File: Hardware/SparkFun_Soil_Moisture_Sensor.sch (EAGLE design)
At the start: 16 parts, among them J1 GATORGATOR_MINI, J2 GATORGATOR_MINI, J3 GATORGATOR_MINI, Q1 2N3904

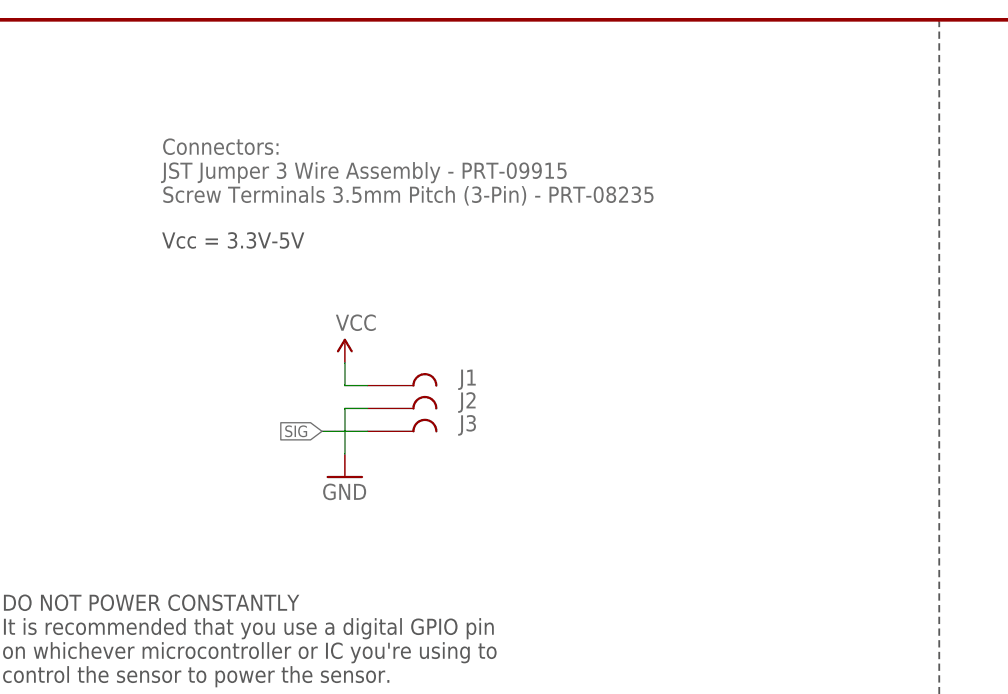
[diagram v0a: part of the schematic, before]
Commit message: adding protection circuitry
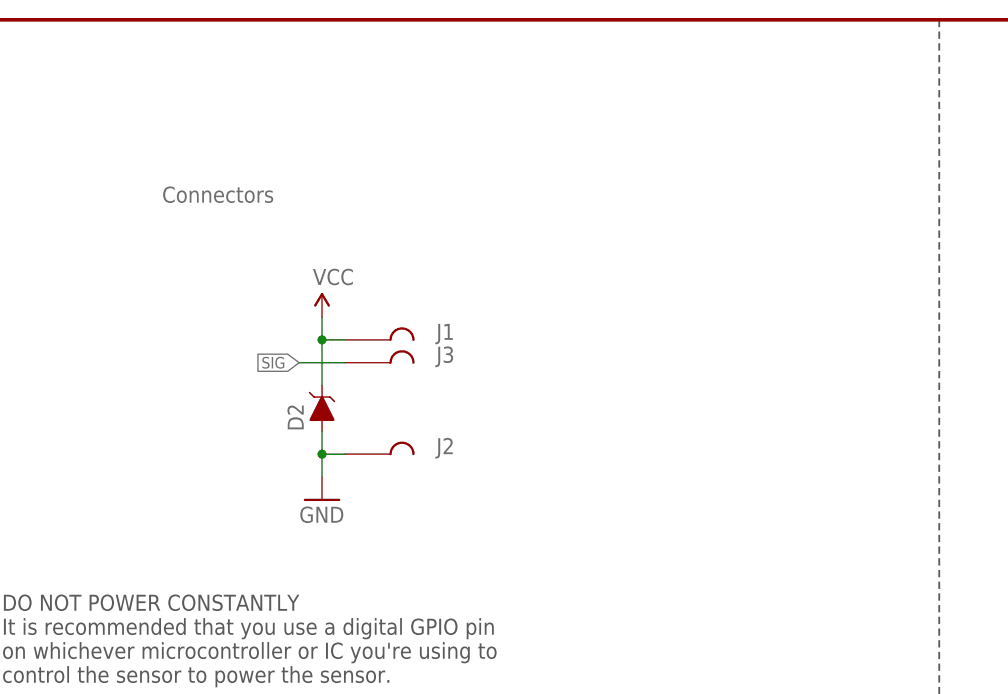
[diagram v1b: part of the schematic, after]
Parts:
- added D2: 3.6V, SparkFun-DiscreteSemi:DIODE-ZENER-BZT52C3V6S
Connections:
- net GND: now also D2.A
- net VCC: now also D2.C
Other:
- note added: "Connectors"
- note removed: "Connectors: JST Jumper 3 Wire Assembly - PRT-09915 Screw Terminals 3.5mm Pitch (3-Pin) - PRT-08235"
- note removed: "Vcc = 3.3V-5V"
- moved on the sheet: J1, J2, J3
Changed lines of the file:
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@@
 <part name="FID4" library="SparkFun-Aesthetics" deviceset="FIDUCIAL" device="1X2"/>
 <part name="LOGO3" library="SparkFun-Aesthetics" deviceset="REVISION" device=""/>
+<part name="D2" library="SparkFun-DiscreteSemi" deviceset="DIODE-ZENER" device="-BZT52C3V6S" value="3.6V"/>
 </parts>
 <sheets>
@@
 The big variable is the composition of the soil itself (especially salts), so ideally you would calibrate for each type of soil.
 -Rob Faludi</text>
-<text x="30.48" y="165.1" size="1.778" layer="95" font="vector">Connectors:
-JST Jumper 3 Wire Assembly - PRT-09915
-Screw Terminals 3.5mm Pitch (3-Pin) - PRT-08235</text>
+<text x="30.48" y="165.1" size="1.778" layer="95" font="vector">Connectors</text>
 <text x="167.64" y="172.72" size="1.778" layer="95" font="vector">Probe Circuit</text>
-<text x="30.48" y="160.02" size="1.778" layer="97" font="vector">Vcc = 3.3V-5V</text>
 <text x="12.7" y="111.76" size="1.778" layer="97" font="vector">DO NOT POWER CONSTANTLY
 It is recommended that you use a digital GPIO pin
@@
 <attribute name="VALUE" x="184.404" y="161.036" size="1.778" layer="96" font="vector"/>
 </instance>
-<instance part="SUPPLY3" gate="G$1" x="50.8" y="147.32" smashed="yes">
-<attribute name="VALUE" x="49.784" y="150.876" size="1.778" layer="96" font="vector"/>
+<instance part="SUPPLY3" gate="G$1" x="48.26" y="152.4" smashed="yes">
+<attribute name="VALUE" x="47.244" y="155.956" size="1.778" layer="96" font="vector"/>
 </instance>
-<instance part="GND2" gate="1" x="50.8" y="134.62" smashed="yes">
-<attribute name="VALUE" x="48.26" y="132.08" size="1.778" layer="96" font="vector"/>
+<instance part="GND2" gate="1" x="48.26" y="132.08" smashed="yes">
+<attribute name="VALUE" x="45.72" y="129.54" size="1.778" layer="96" font="vector"/>
 </instance>
 <instance part="FRAME1" gate="G$1" x="0" y="0" smashed="yes"/>
@@
 <instance part="FID1" gate="G$1" x="137.16" y="27.94" smashed="yes"/>
 <instance part="FID2" gate="G$1" x="142.24" y="27.94" smashed="yes"/>
-<instance part="J1" gate="G$1" x="55.88" y="144.78" smashed="yes">
-<attribute name="NAME" x="63.5" y="144.78" size="1.778" layer="95" font="vector"/>
+<instance part="J1" gate="G$1" x="53.34" y="149.86" smashed="yes">
+<attribute name="NAME" x="60.96" y="149.86" size="1.778" layer="95" font="vector"/>
 </instance>
-<instance part="J2" gate="G$1" x="55.88" y="142.24" smashed="yes">
-<attribute name="NAME" x="63.5" y="142.24" size="1.778" layer="95" font="vector"/>
+<instance part="J2" gate="G$1" x="53.34" y="137.16" smashed="yes">
+<attribute name="NAME" x="60.96" y="137.16" size="1.778" layer="95" font="vector"/>
 </instance>
-<instance part="J3" gate="G$1" x="55.88" y="139.7" smashed="yes">
-<attribute name="NAME" x="63.5" y="139.7" size="1.778" layer="95" font="vector"/>
+<instance part="J3" gate="G$1" x="53.34" y="147.32" smashed="yes">
+<attribute name="NAME" x="60.96" y="147.32" size="1.778" layer="95" font="vector"/>
 </instance>
 <instance part="FID3" gate="G$1" x="137.16" y="22.86" smashed="yes"/>
 <instance part="FID4" gate="G$1" x="142.24" y="22.86" smashed="yes"/>
 <instance part="LOGO3" gate="G$1" x="148.59" y="7.366" smashed="yes"/>
+<instance part="D2" gate="G$1" x="48.26" y="142.24" smashed="yes" rot="R90">
+<attribute name="NAME" x="46.228" y="139.7" size="1.778" layer="95" font="vector" rot="R90"/>
+</instance>
 </instances>
 <busses>
@@
 </segment>
 <segment>
-<wire x1="53.34" y1="139.7" x2="48.26" y2="139.7" width="0.1524" layer="91"/>
-<label x="48.26" y="139.7" size="1.27" layer="95" font="vector" rot="R180" xref="yes"/>
+<label x="45.72" y="147.32" size="1.27" layer="95" font="vector" rot="R180" xref="yes"/>
 <pinref part="J3" gate="G$1" pin="P$1"/>
+<wire x1="50.8" y1="147.32" x2="45.72" y2="147.32" width="0.1524" layer="91"/>
 </segment>
 </net>
@@
 <segment>
 <pinref part="SUPPLY3" gate="G$1" pin="VCC"/>
-<wire x1="53.34" y1="144.78" x2="50.8" y2="144.78" width="0.1524" layer="91"/>
-<wire x1="50.8" y1="144.78" x2="50.8" y2="147.32" width="0.1524" layer="91"/>
+<wire x1="50.8" y1="149.86" x2="48.26" y2="149.86" width="0.1524" layer="91"/>
+<wire x1="48.26" y1="149.86" x2="48.26" y2="152.4" width="0.1524" layer="91"/>
 <pinref part="J1" gate="G$1" pin="P$1"/>
+<pinref part="D2" gate="G$1" pin="C"/>
+<wire x1="48.26" y1="149.86" x2="48.26" y2="144.78" width="0.1524" layer="91"/>
+<junction x="48.26" y="149.86"/>
 </segment>
 <segment>
@@
 <segment>
 <pinref part="J2" gate="G$1" pin="P$1"/>
-<wire x1="53.34" y1="142.24" x2="50.8" y2="142.24" width="0.1524" layer="91"/>
 <pinref part="GND2" gate="1" pin="GND"/>
-<wire x1="50.8" y1="142.24" x2="50.8" y2="137.16" width="0.1524" layer="91"/>
+<wire x1="50.8" y1="137.16" x2="48.26" y2="137.16" width="0.1524" layer="91"/>
+<wire x1="48.26" y1="137.16" x2="48.26" y2="134.62" width="0.1524" layer="91"/>
+<pinref part="D2" gate="G$1" pin="A"/>
+<wire x1="48.26" y1="139.7" x2="48.26" y2="137.16" width="0.1524" layer="91"/>
+<junction x="48.26" y="137.16"/>
 </segment>
 </net>

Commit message: finalizing silk and schematic before design review
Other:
- note added: "v01"
- note removed: "Test different values for R1 to get lower power consumption while still getting a good ADC reading."
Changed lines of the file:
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@@
 <?xml version="1.0" encoding="utf-8"?>
 <!DOCTYPE eagle SYSTEM "eagle.dtd">
-<eagle version="9.3.1">
+<eagle version="9.1.0">
 <drawing>
 <settings>
@@
 <sheet>
 <plain>
-<text x="121.92" y="99.06" size="1.778" layer="97" font="vector">Test different values for R1 to get
-lower power consumption while still getting a good ADC reading. </text>
 <wire x1="0" y1="93.98" x2="116.84" y2="93.98" width="0.2032" layer="97" style="shortdash"/>
 <wire x1="116.84" y1="93.98" x2="248.92" y2="93.98" width="0.2032" layer="97" style="shortdash"/>
@@
 The big variable is the composition of the soil itself (especially salts), so ideally you would calibrate for each type of soil.
 -Rob Faludi</text>
-<text x="30.48" y="165.1" size="1.778" layer="95" font="vector">Connectors</text>
+<text x="43.18" y="167.64" size="1.778" layer="95" font="vector">Connectors</text>
 <text x="167.64" y="172.72" size="1.778" layer="95" font="vector">Probe Circuit</text>
 <text x="12.7" y="111.76" size="1.778" layer="97" font="vector">DO NOT POWER CONSTANTLY
@@
 http://www.dfrobot.com/index.php?route=product/product&amp;product_id=599</text>
 <text x="168.91" y="7.366" size="2.54" layer="94" font="vector">Andy England</text>
+<text x="236.22" y="7.62" size="2.54" layer="94" font="vector">v01</text>
 </plain>
 <instances>
@@
 <attribute name="DRAWING_NAME" x="162.814" y="17.78" size="2.7432" layer="94" font="vector"/>
 <attribute name="DESIGNER" x="166.37" y="11.43" size="2.54" layer="94" font="vector"/>
-<attribute name="VERSION" x="236.22" y="6.35" size="2.54" layer="94" font="vector"/>
 </instance>
 <instance part="LOGO1" gate="G$1" x="88.9" y="0" smashed="yes"/>

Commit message: engineer run of checklist
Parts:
- R1: device SparkFun-Resistors:100OHM-1/4W-5%(0603) -> SparkFun-Resistors:10KOHM-0603-1/10W-1%
- R2: device SparkFun-Resistors:100OHM-1/4W-5%(0603) -> SparkFun-Resistors:100OHM-0603-1/4W-5%
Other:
- note added: "VIN: 3.3-5 V"
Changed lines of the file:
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@@
 <parts>
 <part name="Q1" library="SparkFun-DiscreteSemi" deviceset="TRANSISTOR_NPN" device="MMBT2222A" value="2N3904"/>
-<part name="R1" library="SparkFun-Resistors" deviceset="100OHM-1/4W-5%(0603)" device="" value="10k"/>
+<part name="R1" library="SparkFun-Resistors" deviceset="10KOHM" device="-0603-1/10W-1%" value="10k"/>
 <part name="SUPPLY1" library="SparkFun-Aesthetics" deviceset="VCC" device=""/>
 <part name="GND1" library="SparkFun-Aesthetics" deviceset="GND" device=""/>
-<part name="R2" library="SparkFun-Resistors" deviceset="100OHM-1/4W-5%(0603)" device="" value="100"/>
+<part name="R2" library="SparkFun-Resistors" deviceset="100OHM" device="-0603-1/4W-5%" value="100"/>
 <part name="SUPPLY2" library="SparkFun-Aesthetics" deviceset="VCC" device=""/>
 <part name="SUPPLY3" library="SparkFun-Aesthetics" deviceset="VCC" device=""/>
@@
 <text x="168.91" y="7.366" size="2.54" layer="94" font="vector">Andy England</text>
 <text x="236.22" y="7.62" size="2.54" layer="94" font="vector">v01</text>
+<text x="167.64" y="170.18" size="1.778" layer="97" font="vector">VIN: 3.3-5 V</text>
 </plain>
 <instances>

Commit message: updating 100 ohm resistor
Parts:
- R2: device SparkFun-Resistors:100OHM-0603-1/4W-5% -> SparkFun-Resistors:100OHM-0603-1/10W-1%
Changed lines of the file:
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@@
 <part name="SUPPLY1" library="SparkFun-Aesthetics" deviceset="VCC" device=""/>
 <part name="GND1" library="SparkFun-Aesthetics" deviceset="GND" device=""/>
-<part name="R2" library="SparkFun-Resistors" deviceset="100OHM" device="-0603-1/4W-5%" value="100"/>
+<part name="R2" library="SparkFun-Resistors" deviceset="100OHM" device="-0603-1/10W-1%" value="100"/>
 <part name="SUPPLY2" library="SparkFun-Aesthetics" deviceset="VCC" device=""/>
 <part name="SUPPLY3" library="SparkFun-Aesthetics" deviceset="VCC" device=""/>

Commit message: engineer run of checklist
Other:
- note added: "VCC: 3.3-5 V"
- note added: "v10"
- note removed: "VIN: 3.3-5 V"
- note removed: "v01"
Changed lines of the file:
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@@
 http://www.dfrobot.com/index.php?route=product/product&amp;product_id=599</text>
 <text x="168.91" y="7.366" size="2.54" layer="94" font="vector">Andy England</text>
-<text x="236.22" y="7.62" size="2.54" layer="94" font="vector">v01</text>
-<text x="167.64" y="170.18" size="1.778" layer="97" font="vector">VIN: 3.3-5 V</text>
+<text x="236.22" y="7.62" size="2.54" layer="94" font="vector">v10</text>
+<text x="167.64" y="170.18" size="1.778" layer="97" font="vector">VCC: 3.3-5 V</text>
 </plain>
 <instances>
